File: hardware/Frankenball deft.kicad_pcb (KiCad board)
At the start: 2 copper layers, 50.5 x 62 mm, 38 parts, among them J1 Conn_02x03_Odd_Even, J2 Connector_Generic:Conn_01x05, J52 PWM3320, J53 Conn_01x04_Male, J54 Conn_01x12, J55 Conn_01x05_Female, SW1 SW_Push, SW51 SW_Push, U1 XC6206PxxxMR, U2 STM32F411CCUx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

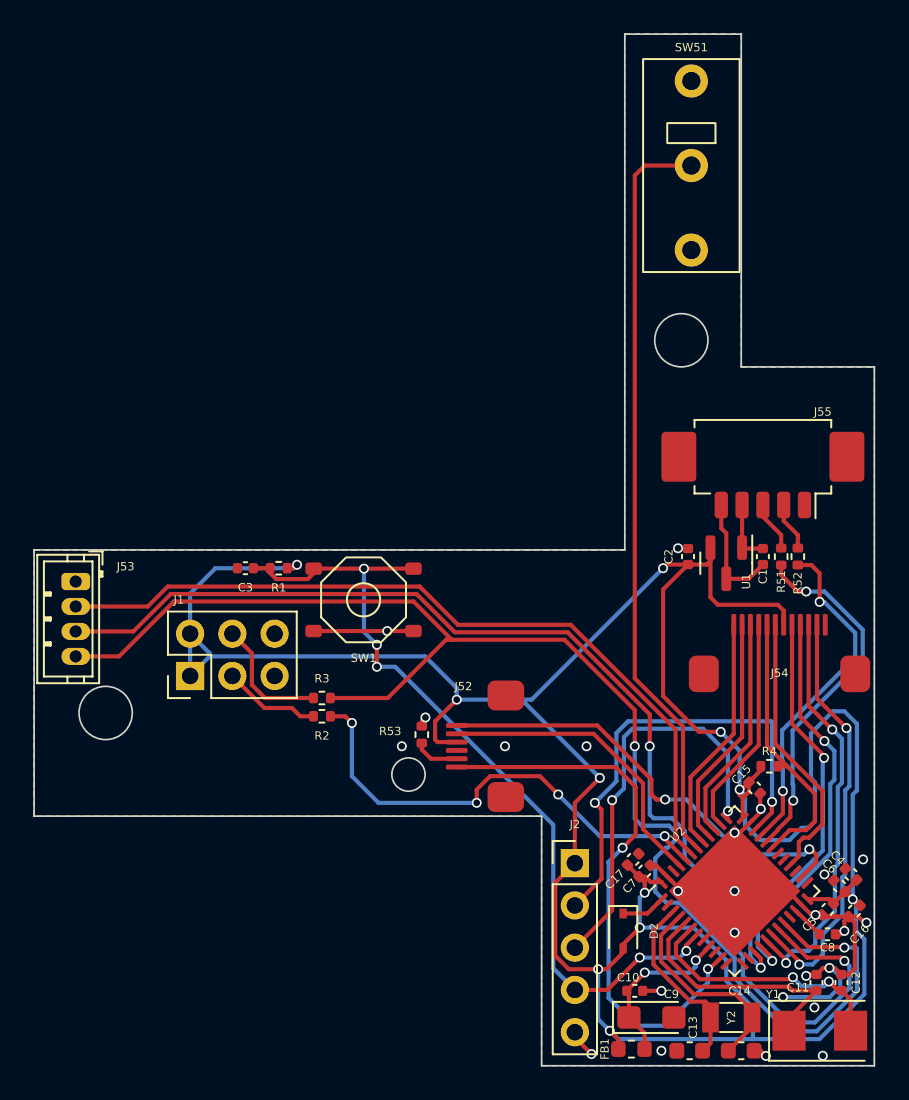
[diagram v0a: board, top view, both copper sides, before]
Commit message: Replace boot config header with PFET
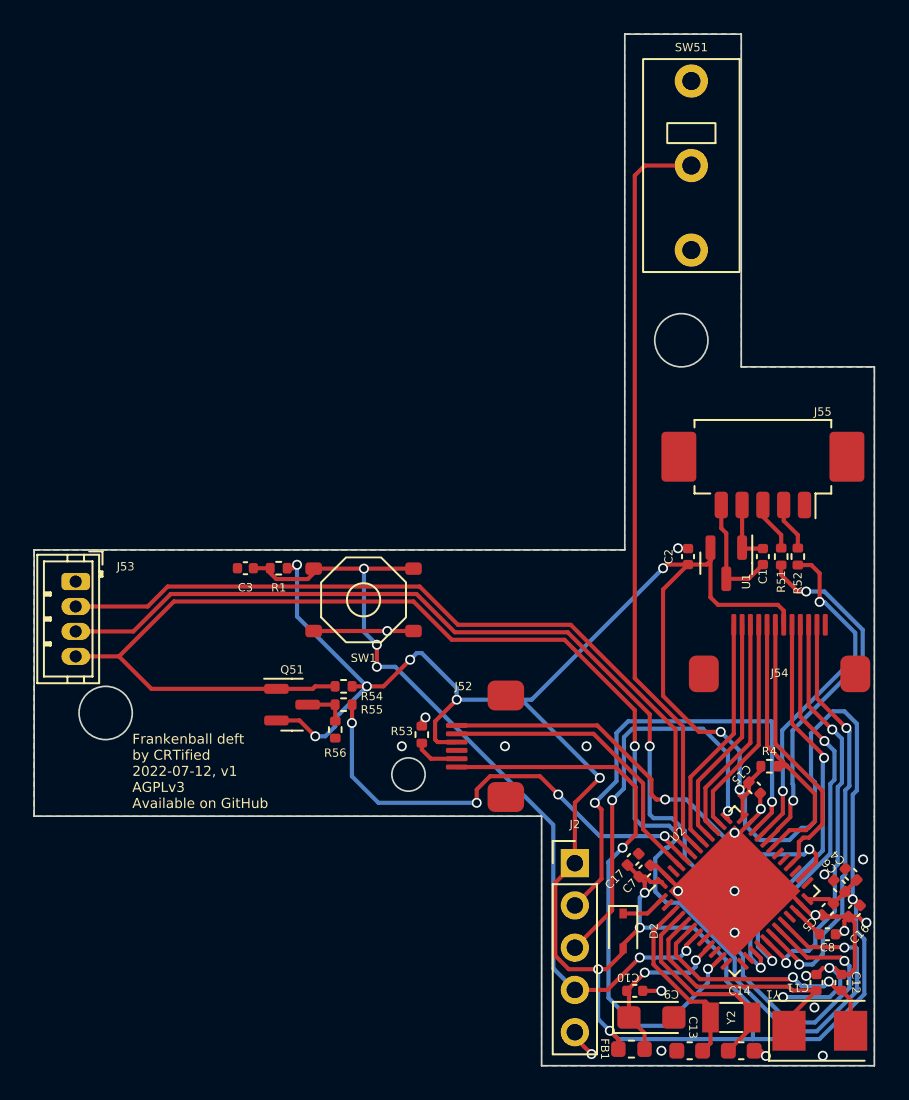
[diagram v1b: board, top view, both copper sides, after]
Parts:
- removed J1: Conn_02x03_Odd_Even, Connector_PinHeader_2.54mm:PinHeader_2x03_P2.54mm_Vertical
- removed R2, R3: 10k, Resistor_SMD:R_0402_1005Metric
- added Q51: AO3401A, Package_TO_SOT_SMD:SOT-23, F.Cu at (170.0, 138.3)
- added R54: 10k, Resistor_SMD:R_0402_1005Metric, F.Cu at (173.1, 137.2)
- added R55: 10k, Resistor_SMD:R_0402_1005Metric, F.Cu at (173.1, 138.3)
- added R56: 10k, Resistor_SMD:R_0402_1005Metric, F.Cu at (172.6, 139.8)
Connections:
- U2 pad 44: /STM32F411/BOOT0 -> /BOOT0
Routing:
- net /STM32F411/BOOT0: track 28.7 -> 0.00 mm, vias 4 -> 0
- net /BOOT0: track 0.00 -> 28.3 mm, vias 0 -> 4
- net Net-(J1-Pad4): track 7.59 -> 0.00 mm
- net +3V3: track 189.7 -> 182.8 mm, vias 11 -> 14
- net Net-(J1-Pad3): track 5.88 -> 0.00 mm
- net /STM32F411/PB2: track 84.7 -> 89.9 mm
- net Net-(Q51-Pad3): track 0.00 -> 2.65 mm
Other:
- board text added: "Frankenball deft by CRTified 2022-07-12, v1 AGPLv3 Available on GitHub"

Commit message: Add fabrication files
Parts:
- moved C11 0.66 mm to (201.0, 155.4), turned to 0 degrees
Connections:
- net +3V3 renamed +3.3V
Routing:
- net GND: track 52.5 -> 50.0 mm, vias 25 -> 23
- net /STM32F411/XTAL_8M_1: track 15.4 -> 14.0 mm
- net /STM32F411/XTAL_8M_2: track 15.8 -> 15.6 mm, vias 2 -> 0
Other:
- board text added: "JLCJLCJLCJLC"
